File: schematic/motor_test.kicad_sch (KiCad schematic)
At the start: 27 parts

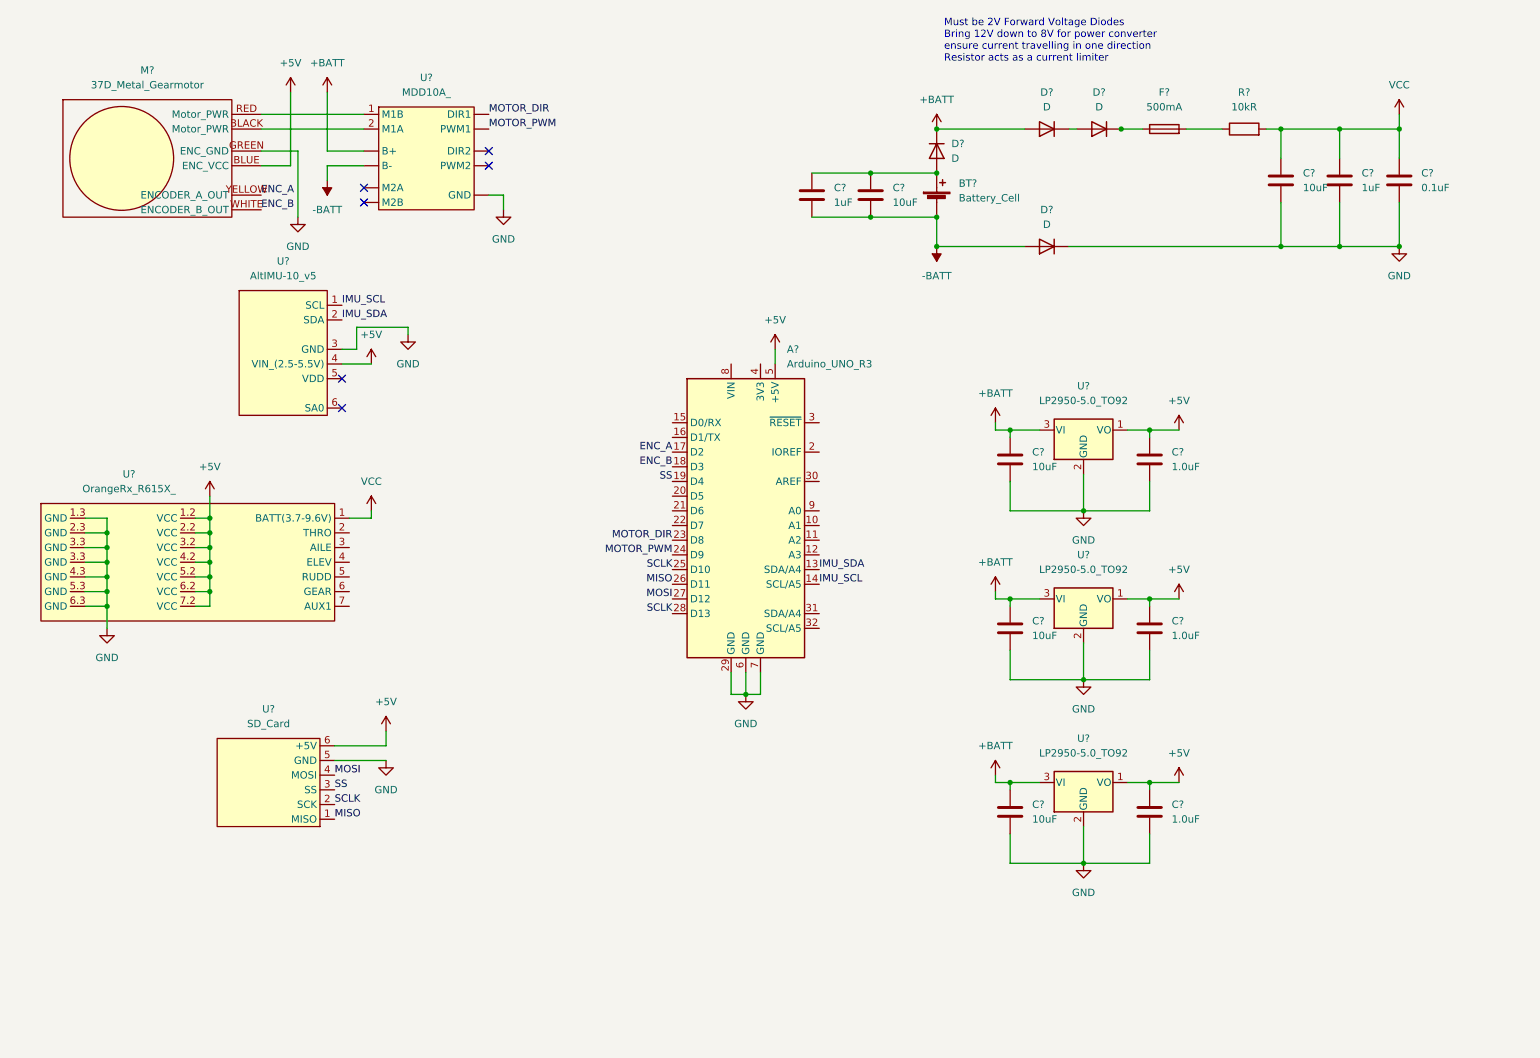
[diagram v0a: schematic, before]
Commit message: removed uneccessary stuff from schematic
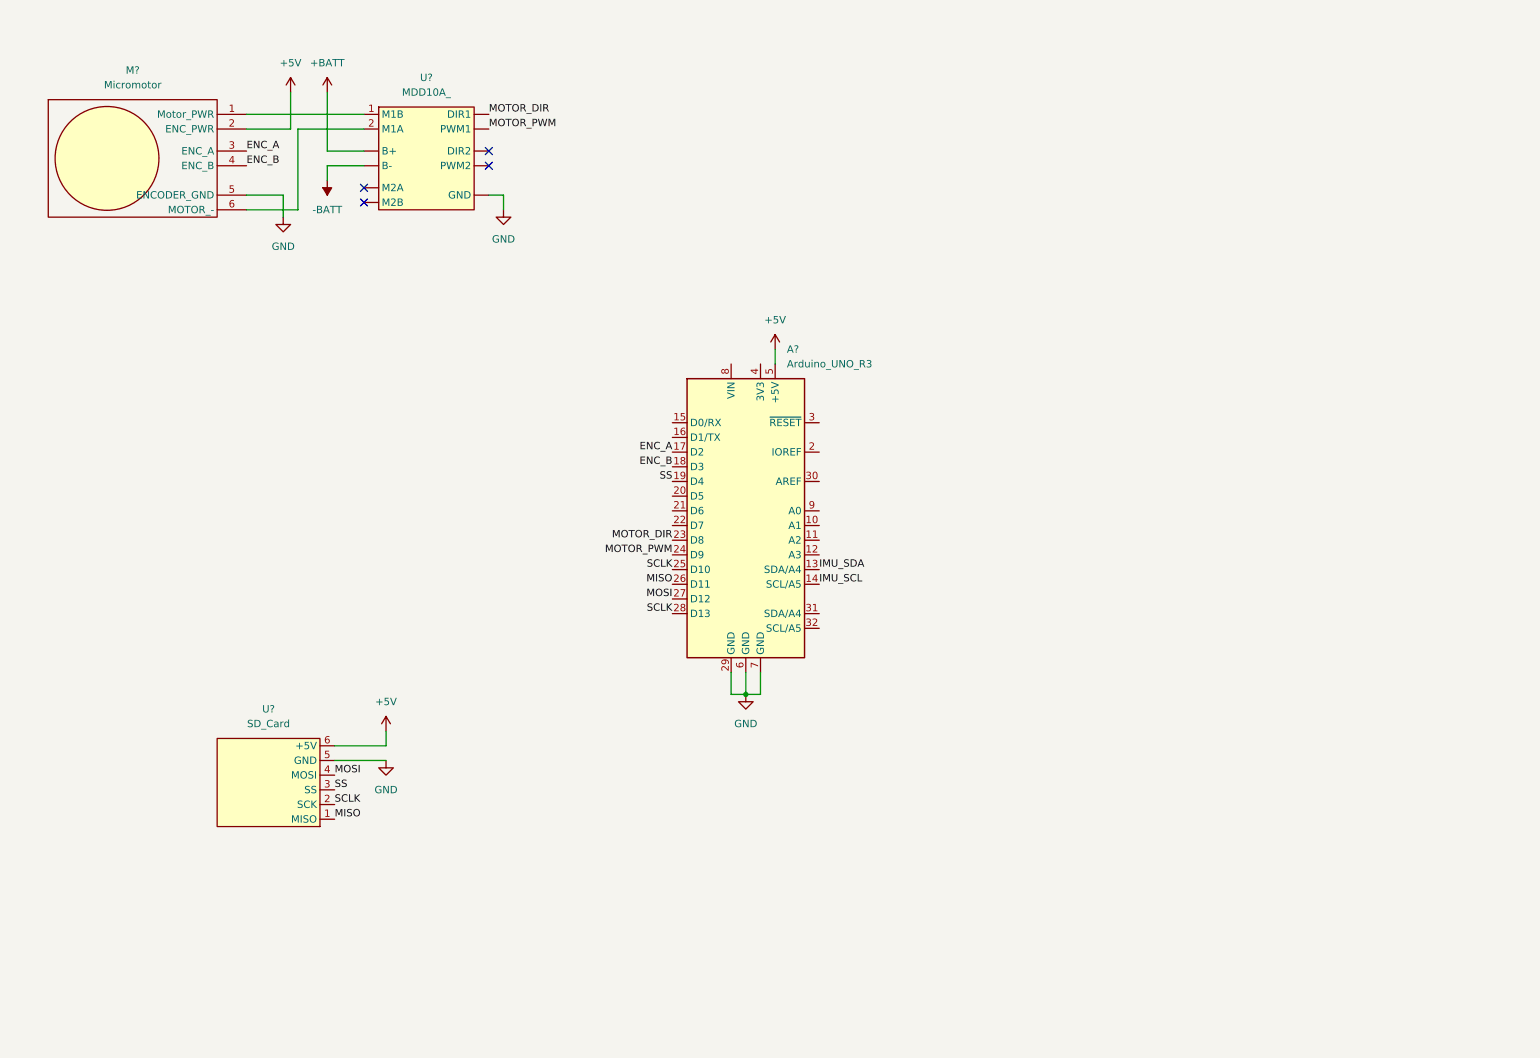
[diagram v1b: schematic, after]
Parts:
- removed BT?: Battery_Cell, symbol Device:Battery_Cell
- removed C? (x5): 10uF, symbol Device:C
- removed C? (x3): 1.0uF, symbol Device:C
- removed C?: 0.1uF, symbol Device:C
- removed C? (x2): 1uF, symbol Device:C
- removed D? (x4): D, symbol Device:D
- removed F?: 500mA, symbol Device:Fuse
- removed M?: 37D_Metal_Gearmotor, symbol rogallo_wing_test_lib:37D_Metal_Gearmotor
- removed R?: 10kR, symbol Device:R
- removed U? (x3): LP2950-5.0_TO92, Package_TO_SOT_THT:TO-92_Inline, symbol Regulator_Linear:LP2950-5.0_TO92
- removed U?: OrangeRx_R615X_, symbol rogallo_wing_test_lib:OrangeRx_R615X_
- removed U?: AltIMU-10_v5, symbol rogallo_wing_test_lib:AltIMU-10_v5
- added M?: Micromotor, symbol rogallo_wing_test_lib:Micromotor
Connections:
- net +5V: now also M?.2 (ENC_PWR)
- net ENC_A: now also M?.3 (ENC_A)
- net ENC_B: now also M?.4 (ENC_B)
- net GND: now also M?.5 (ENCODER_GND)
- net at U?.1 (M1B): now also M?.1 (Motor_PWR)
- net at U?.2 (M1A): now also M?.6 (MOTOR_-)
- no-connect marks 6 -> 4
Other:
- note removed: "Must be 2V Forward Voltage Diodes Bring 12V down to 8V for power converter ensure current travelling in one direction Resistor acts as a current limiter"

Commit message: cheap sensors
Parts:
- removed U?: MDD10A_, symbol rogallo_wing_test_lib:MDD10A_
- added M? (x3): Micromotor, symbol rogallo_wing_test_lib:Micromotor
- added U? (x2): TB6612FNG, Package_SO:SSOP-24_5.3x8.2mm_P0.65mm, symbol Driver_Motor:TB6612FNG
- added U?: HC-SR04, symbol rogallo_wing_test_lib:HC-SR04
- added U?: MPU-9250, Sensor_Motion:InvenSense_QFN-24_3x3mm_P0.4mm, symbol Sensor_Motion:MPU-9250
- added U?: GP2Y0A21YK0F, symbol rogallo_wing_test_lib:GP2Y0A21YK0F
- added U?: VL53L1CXV0FY1, Sensor_Distance:ST_VL53L1x, symbol Sensor_Distance:VL53L1CXV0FY1
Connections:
- net +5V: now also M?.2 (ENC_PWR), M?.2 (ENC_PWR), M?.2 (ENC_PWR), U?.1 (VCC), U?.19 (STBY), U?.19 (STBY), U?.20 (VCC), U?.20 (VCC), U?.RED (PWR)
- net +BATT: now also A?.8 (VIN), U?.13 (VM2), U?.13 (VM2), U?.14 (VM3), U?.14 (VM3), U?.24 (VM1), U?.24 (VM1)
- net GND: now also M?.5 (ENCODER_GND), M?.5 (ENCODER_GND), M?.5 (ENCODER_GND), U?.10 (PGND2), U?.10 (PGND2), U?.12 (INT), U?.18 (GND), U?.18 (GND), U?.18 (GND), U?.22 (~{CS}), U?.3 (PGND1), U?.3 (PGND1), U?.4 (GND), U?.4 (PGND1), U?.4 (PGND1), U?.9 (PGND2), U?.9 (PGND2), U?.BLK (GND)
- net MISO: no longer A?.26 (D11)
- net MOSI: no longer A?.27 (D12)
- net SCLK: no longer A?.25 (D10), A?.28 (D13)
- net SS: no longer A?.19 (D4)
- net ULTRA: now reaches A?.10 (A1)
- net ULTRA: now also U?.WHT (OUT)
- net BIN2_M2: now reaches A?.11 (A2)
- net BIN2_M2: now also A?.12 (A3), U?.16 (BIN2), U?.16 (BIN2), U?.17 (BIN1), U?.17 (BIN1)
- net trig: now reaches A?.20 (D5)
- net trig: now also U?.2 (Trig)
- net PWM_M3: now reaches A?.21 (D6)
- net PWM_M3: now also U?.23 (PWMA)
- net ENCB_M2: now reaches A?.22 (D7)
- net ENCB_M2: now also M?.4 (ENC_B)
- net +3V3: now reaches A?.4 (3V3)
- net +3V3: now also U?.13 (VDD), U?.8 (VDDIO)
- net PWR_M1: now reaches M?.1 (Motor_PWR)
- net PWR_M1: now also U?.1 (AO1), U?.2 (AO1)
- net NEG_M1: now reaches M?.6 (MOTOR_-)
- net NEG_M1: now also U?.5 (AO2), U?.6 (AO2)
- net ENC_A renamed AIN1_M1
- net AIN1_M1: now also U?.21 (AIN1), U?.21 (AIN1); no longer M?.3 (ENC_A)
- net ENC_B renamed AIN2_M1
- net AIN2_M1: now also U?.22 (AIN2), U?.22 (AIN2); no longer M?.4 (ENC_B)
- net IMU_SCL renamed SCL
- net SCL: now also U?.7 (AUX_SCL)
- net IMU_SDA renamed SDA
- net SDA: now also U?.21 (AUX_SDA)
- net MOTOR_DIR renamed ENCA_M2
- net ENCA_M2: now also M?.3 (ENC_A)
- net MOTOR_PWM renamed PWM_M4
- net PWM_M4: now also U?.15 (PWMB)
- new net: U?.12 (GND), U?.3 (GND), U?.4 (GND), U?.6 (GND)
- new net ENCA_M1: A?.28 (D13), M?.3 (ENC_A)
- new net ENCB_M1: A?.27 (D12), M?.4 (ENC_B)
- new net NEG_M2: M?.6 (MOTOR_-), U?.7 (BO2), U?.8 (BO2)
- new net NEG_M3: U?.5 (AO2), U?.6 (AO2)
- new net NEG_M4: M?.6 (MOTOR_-), M?.6 (MOTOR_-), U?.7 (BO2), U?.8 (BO2)
- new net PWM_M1: A?.25 (D10), U?.23 (PWMA)
- new net PWM_M2: A?.26 (D11), U?.15 (PWMB)
- new net PWR_M2: M?.1 (Motor_PWR), U?.11 (BO1), U?.12 (BO1)
- new net PWR_M3: M?.1 (Motor_PWR), U?.1 (AO1), U?.2 (AO1)
- new net PWR_M4: M?.1 (Motor_PWR), U?.11 (BO1), U?.12 (BO1)
- new net echo: A?.19 (D4), U?.3 (Echo)
- no-connect marks 4 -> 11
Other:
- note added: "Control Direction"
- note added: "Control Speed"
- note added: "Controls speed of 4 motors independantly, but direction of motors controlled in pairs"
- note added: "IMU: GYROMETER, ACCELEROMETER, MAGNOMETOR"
- note added: "IR Distance Sensor"
- note added: "ROB-14451 breakout board used to interface with half bridge TB6612FNG Two half bridges are used for each motor"
- note added: "SD Card: Log test data"
- note added: "Signals to motors"
- note added: "Ultrasonic Sensor:"
- moved on the sheet: A?, M?, U?
